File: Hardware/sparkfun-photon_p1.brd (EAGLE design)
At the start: 68.6 x 53.3 mm, 51 parts, among them U1 WM-N-BM-14

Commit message: Renaming extra pins to S1-S6 (SPARE).
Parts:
- moved LOGO1 3.29 mm to (28.4, 23.0)
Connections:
- net D0 renamed D0/SDA
- net D1 renamed D1/SCL
- net PB0 renamed SPARE1
- net PB1 renamed SPARE2
- net PC0 renamed SPARE3
- net PC1 renamed SPARE6
- net PC13 renamed SPARE5
- net PC4 renamed SPARE4
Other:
- board text added: "Photon RedBoard"
- board text added: "S1"
- board text added: "S2"
- board text added: "S3"
- board text added: "S4"
- board text added: "S5"
- board text added: "S6"
- board text removed: "B0"
- board text removed: "B1"
- board text removed: "C0"
- board text removed: "C1"
- board text removed: "C4"
- board text removed: "Cd"
- board text removed: "Photon P1R3"
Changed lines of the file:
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@@
 <text x="20.32" y="22.225" size="1.27" layer="21" font="vector" ratio="15" rot="R180" align="center-left">D7</text>
 <text x="20.32" y="10.795" size="1.27" layer="21" font="vector" ratio="15" rot="R180" align="center-left">POWER</text>
-<text x="18.796" y="28.067" size="1.778" layer="21" font="vector" ratio="15" align="top-left">Photon P1R3</text>
+<text x="18.796" y="28.067" size="1.27" layer="21" font="vector" ratio="15" align="top-left">Photon RedBoard</text>
 <text x="9.652" y="29.337" size="1.524" layer="21" font="vector" ratio="15" rot="R90" align="top-center">MODE</text>
 <text x="9.652" y="48.387" size="1.524" layer="21" font="vector" ratio="15" rot="R90" align="top-center">RESET</text>
 <wire x1="41.275" y1="40.259" x2="42.545" y2="40.259" width="0.2032" layer="21"/>
-<text x="49.53" y="9.144" size="1.016" layer="21" font="vector" ratio="15" rot="R90" align="center-left">B0</text>
-<text x="52.07" y="9.144" size="1.016" layer="21" font="vector" ratio="15" rot="R90" align="center-left">B1</text>
-<text x="54.61" y="9.144" size="1.016" layer="21" font="vector" ratio="15" rot="R90" align="center-left">C0</text>
-<text x="57.15" y="9.144" size="1.016" layer="21" font="vector" ratio="15" rot="R90" align="center-left">C4</text>
-<text x="59.69" y="9.144" size="1.016" layer="21" font="vector" ratio="15" rot="R90" align="center-left">Cd</text>
-<text x="62.23" y="9.144" size="1.016" layer="21" font="vector" ratio="15" rot="R90" align="center-left">C1</text>
+<text x="49.53" y="9.144" size="1.016" layer="21" font="vector" ratio="15" rot="R90" align="center-left">S1</text>
+<text x="52.07" y="9.144" size="1.016" layer="21" font="vector" ratio="15" rot="R90" align="center-left">S2</text>
+<text x="54.61" y="9.144" size="1.016" layer="21" font="vector" ratio="15" rot="R90" align="center-left">S3</text>
+<text x="57.15" y="9.144" size="1.016" layer="21" font="vector" ratio="15" rot="R90" align="center-left">S4</text>
+<text x="59.69" y="9.144" size="1.016" layer="21" font="vector" ratio="15" rot="R90" align="center-left">S5</text>
+<text x="62.23" y="9.144" size="1.016" layer="21" font="vector" ratio="15" rot="R90" align="center-left">S6</text>
 <wire x1="44.45" y1="52.07" x2="44.45" y2="49.53" width="0.2032" layer="21"/>
 <wire x1="44.45" y1="49.53" x2="64.77" y2="49.53" width="0.2032" layer="21"/>
@@
 </element>
 <element name="LOGO2" library="SparkFun-Aesthetics" package="SFE_LOGO_NAME_FLAME_.2" value="SFE_LOGO_NAME_FLAME.2_INCH" x="13.462" y="27.178"/>
-<element name="LOGO1" library="SparkFun-Aesthetics" package="OSHW-LOGO-M" value="OSHW-LOGOM" x="31.369" y="21.463"/>
+<element name="LOGO1" library="SparkFun-Aesthetics" package="OSHW-LOGO-M" value="OSHW-LOGOM" x="28.448" y="22.987"/>
 <element name="U1" library="sparkfun_photon_temp" package="WM-N-BM-14" value="WM-N-BM-14" x="48.26" y="21.59">
 <attribute name="PROD_ID" value="IC-12589" x="48.26" y="21.59" size="1.778" layer="27" font="vector" ratio="15" display="off"/>
@@
 <wire x1="51.308" y1="21.082" x2="53.34" y2="19.05" width="0.3048" layer="16"/>
 </signal>
-<signal name="D1">
+<signal name="D1/SCL">
 <contactref element="JP5" pad="SCL"/>
 <contactref element="U1" pad="35"/>
@@
 <wire x1="39.37" y1="9.779" x2="36.83" y2="12.319" width="0.3048" layer="16"/>
 <wire x1="36.83" y1="12.319" x2="36.83" y2="19.05" width="0.3048" layer="16"/>
-<via x="29.21" y="26.67" extent="1-16" drill="0.508"/>
-<wire x1="29.21" y1="26.67" x2="18.796" y2="37.084" width="0.3048" layer="1"/>
-<wire x1="36.83" y1="19.05" x2="29.21" y2="26.67" width="0.3048" layer="16"/>
+<via x="31.75" y="24.13" extent="1-16" drill="0.508"/>
+<wire x1="31.75" y1="24.13" x2="18.796" y2="37.084" width="0.3048" layer="1"/>
+<wire x1="36.83" y1="19.05" x2="31.75" y2="24.13" width="0.3048" layer="16"/>
 <wire x1="43.31" y1="12.09" x2="43.31" y2="10.795" width="0.3048" layer="1"/>
 <wire x1="43.31" y1="10.795" x2="43.183" y2="10.668" width="0.3048" layer="1"/>
@@
 <wire x1="42.294" y1="9.779" x2="43.183" y2="10.668" width="0.3048" layer="16"/>
 </signal>
-<signal name="D0">
+<signal name="D0/SDA">
 <contactref element="JP5" pad="SDA"/>
 <contactref element="U1" pad="36"/>
 <via x="43.04" y="13.589" extent="1-16" drill="0.508"/>
 <wire x1="21.336" y1="50.8" x2="21.336" y2="35.814" width="0.3048" layer="1"/>
-<wire x1="21.336" y1="35.814" x2="29.21" y2="27.94" width="0.3048" layer="1"/>
-<via x="29.21" y="27.94" extent="1-16" drill="0.508"/>
-<wire x1="37.465" y1="19.304" x2="30.226" y2="26.543" width="0.3048" layer="16"/>
+<wire x1="21.336" y1="35.814" x2="31.75" y2="25.4" width="0.3048" layer="1"/>
+<via x="31.75" y="25.4" extent="1-16" drill="0.508"/>
+<wire x1="37.465" y1="19.304" x2="32.766" y2="24.003" width="0.3048" layer="16"/>
 <wire x1="37.465" y1="14.605" x2="37.465" y2="19.304" width="0.3048" layer="16"/>
-<wire x1="30.226" y1="26.543" x2="30.226" y2="26.924" width="0.3048" layer="16"/>
-<wire x1="30.226" y1="26.924" x2="29.21" y2="27.94" width="0.3048" layer="16"/>
+<wire x1="32.766" y1="24.003" x2="32.766" y2="24.384" width="0.3048" layer="16"/>
+<wire x1="32.766" y1="24.384" x2="31.75" y2="25.4" width="0.3048" layer="16"/>
 <wire x1="44.31" y1="12.09" x2="44.31" y2="13.094" width="0.3048" layer="1"/>
 <wire x1="44.31" y1="13.094" x2="43.815" y2="13.589" width="0.3048" layer="1"/>
@@
 <wire x1="45.505" y1="8.255" x2="45.505" y2="9.525" width="0.508" layer="1"/>
 </signal>
-<signal name="PB0">
+<signal name="SPARE1">
 <contactref element="U1" pad="40"/>
 <contactref element="JP3" pad="6"/>
@@
 <wire x1="48.31" y1="8.84" x2="49.53" y2="7.62" width="0.3048" layer="1"/>
 </signal>
-<signal name="PB1">
+<signal name="SPARE2">
 <contactref element="U1" pad="41"/>
 <contactref element="JP3" pad="5"/>
@@
 <wire x1="50.673" y1="9.017" x2="52.07" y2="7.62" width="0.3048" layer="1"/>
 </signal>
-<signal name="PC0">
+<signal name="SPARE3">
 <contactref element="U1" pad="42"/>
 <contactref element="JP3" pad="4"/>
@@
 <wire x1="53.213" y1="9.017" x2="54.61" y2="7.62" width="0.3048" layer="1"/>
 </signal>
-<signal name="PC4">
+<signal name="SPARE4">
 <contactref element="U1" pad="44"/>
 <contactref element="JP3" pad="3"/>
@@
 <wire x1="55.118" y1="9.652" x2="57.15" y2="7.62" width="0.3048" layer="1"/>
 </signal>
-<signal name="PC13">
+<signal name="SPARE5">
 <contactref element="U1" pad="47"/>
 <contactref element="JP3" pad="2"/>
@@
 <wire x1="59.69" y1="8.89" x2="59.69" y2="7.62" width="0.3048" layer="1"/>
 </signal>
-<signal name="PC1">
+<signal name="SPARE6">
 <contactref element="U1" pad="48"/>
 <contactref element="JP3" pad="1"/>

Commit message: Adding jumper to disconnect Power LED.
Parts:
- added SJ1: PWR-LED, SparkFun-Passives:PAD-JUMPER-2-NC_BY_TRACE_YES_SILK
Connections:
- new net N$2: LED1.C, SJ1.2
- net GND: now also SJ1.1; no longer LED1.C
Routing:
- net N$2: track 0.00 -> 4.60 mm, vias 0 -> 1
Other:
- board text added: "PWR LED"
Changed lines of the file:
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@@
 <text x="55.245" y="21.59" size="0.8128" layer="22" font="vector" ratio="15" rot="MR0" align="center-right">BTCX-RF_ACT</text>
 <text x="54.483" y="22.59" size="0.8128" layer="22" font="vector" ratio="15" rot="MR0" align="center-right">BTCX-STAT</text>
+<text x="24.003" y="10.795" size="0.8128" layer="22" font="vector" ratio="15" rot="MR0" align="center-right">PWR
+LED</text>
 </plain>
 <attributes>
@@
 <element name="TP9" library="SparkFun-Passives" package="TP_15TH" value="TEST-POINTTP_15TH_THRU" x="54.737" y="25.59" rot="MR0"/>
 <element name="TP10" library="SparkFun-Passives" package="TP_15TH" value="TEST-POINTTP_15TH_THRU" x="41.31" y="10.668"/>
+<element name="SJ1" library="SparkFun-Passives" package="PAD-JUMPER-2-NC_BY_TRACE_YES_SILK" value="PWR-LED" x="22.86" y="10.795" rot="MR0"/>
 </elements>
 <signals>
@@
 <contactref element="S2" pad="1"/>
 <contactref element="LED2" pad="C"/>
-<contactref element="LED1" pad="C"/>
 <polygon width="0.254" layer="16" isolate="0.3048" rank="6">
 <vertex x="0" y="0"/>
@@
 <via x="26.543" y="32.004" extent="1-16" drill="0.508"/>
 <via x="12.573" y="30.861" extent="1-16" drill="0.508"/>
+<contactref element="SJ1" pad="1"/>
 </signal>
 <signal name="3.3V">
@@
 <wire x1="41.31" y1="12.09" x2="41.31" y2="10.668" width="0.3048" layer="1"/>
 </signal>
+<signal name="N$2">
+<contactref element="SJ1" pad="2"/>
+<contactref element="LED1" pad="C"/>
+<wire x1="21.36" y1="10.795" x2="21.36" y2="11.66" width="0.3048" layer="1"/>
+<wire x1="21.36" y1="11.66" x2="20.701" y2="12.319" width="0.3048" layer="1"/>
+<via x="20.701" y="12.319" extent="1-16" drill="0.508"/>
+<wire x1="20.701" y1="12.319" x2="20.701" y2="11.43" width="0.3048" layer="16"/>
+<wire x1="20.701" y1="11.43" x2="21.336" y2="10.795" width="0.3048" layer="16"/>
+<wire x1="21.336" y1="10.795" x2="22.352" y2="10.795" width="0.3048" layer="16"/>
+</signal>
 </signals>
 <errors>
@@
 </board>
 </drawing>
+<compatibility>
+<note version="6.3" minversion="6.2.2" severity="warning">
+Since Version 6.2.2 text objects can contain more than one line,
+which will not be processed correctly with this version.
+</note>
+</compatibility>
 </eagle>

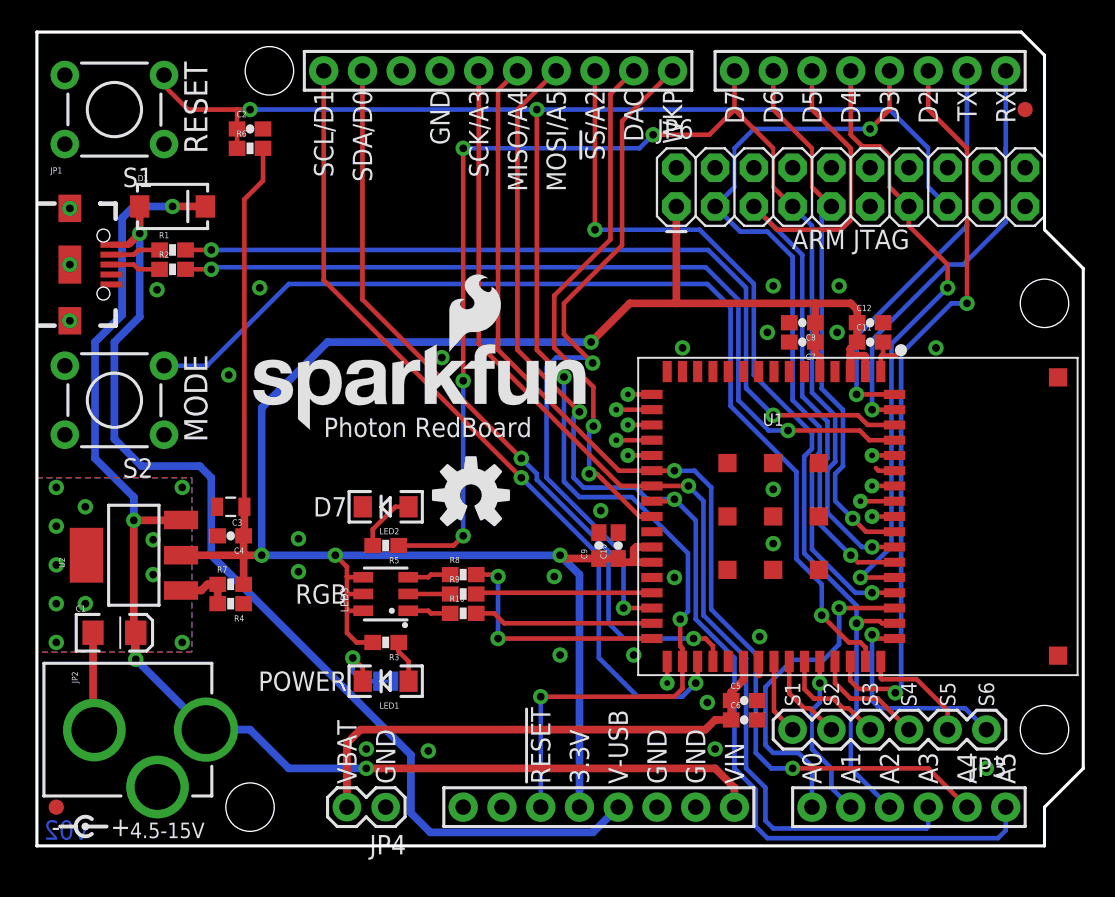
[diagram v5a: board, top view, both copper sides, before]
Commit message: Changing Arduino headers to locking footprints.
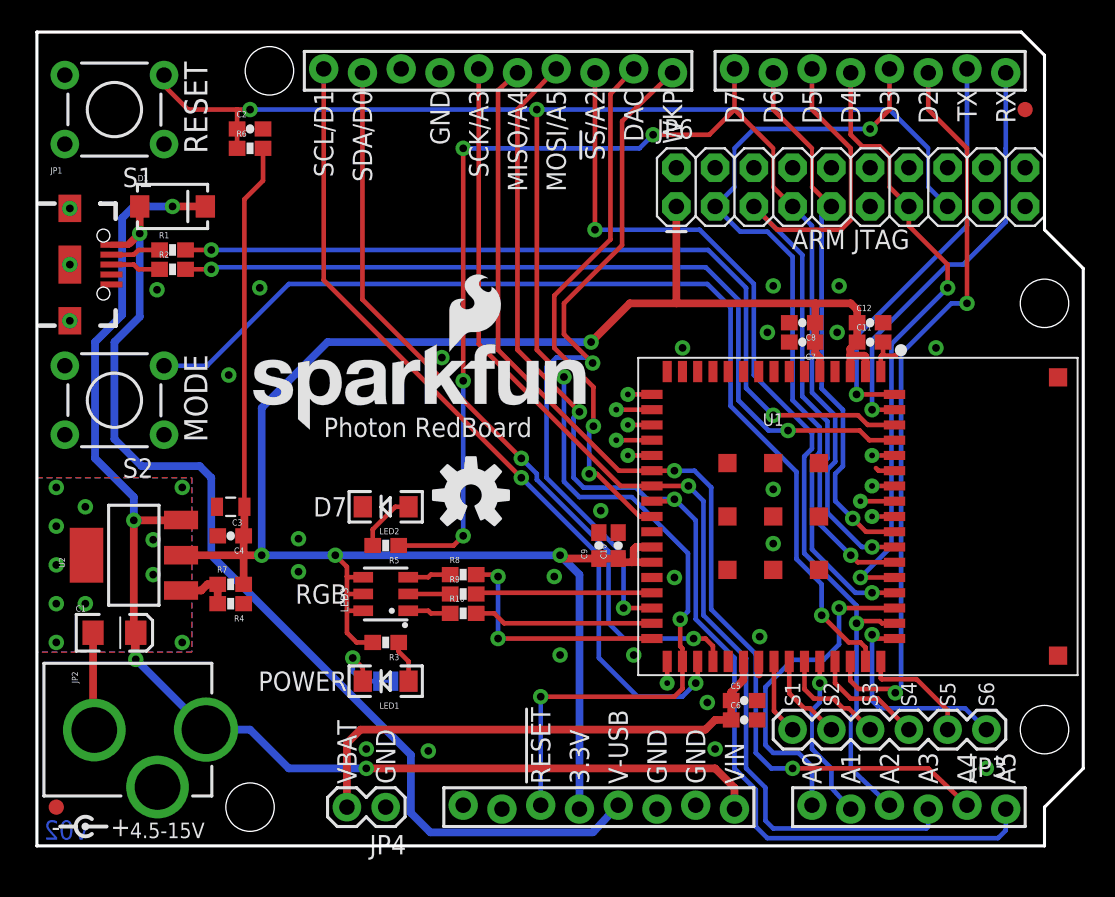
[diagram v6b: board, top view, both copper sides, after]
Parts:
- JP5: value ARDUINO_R3_NOISP -> ARDUINO_R3_NOISPLOCKING; device sparkfun_photon_temp:ARDUINO_R3_NOISP -> sparkfun_photon_temp:ARDUINO_R3_NOISP_LOCKING
